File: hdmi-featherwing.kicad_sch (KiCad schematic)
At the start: 9 parts

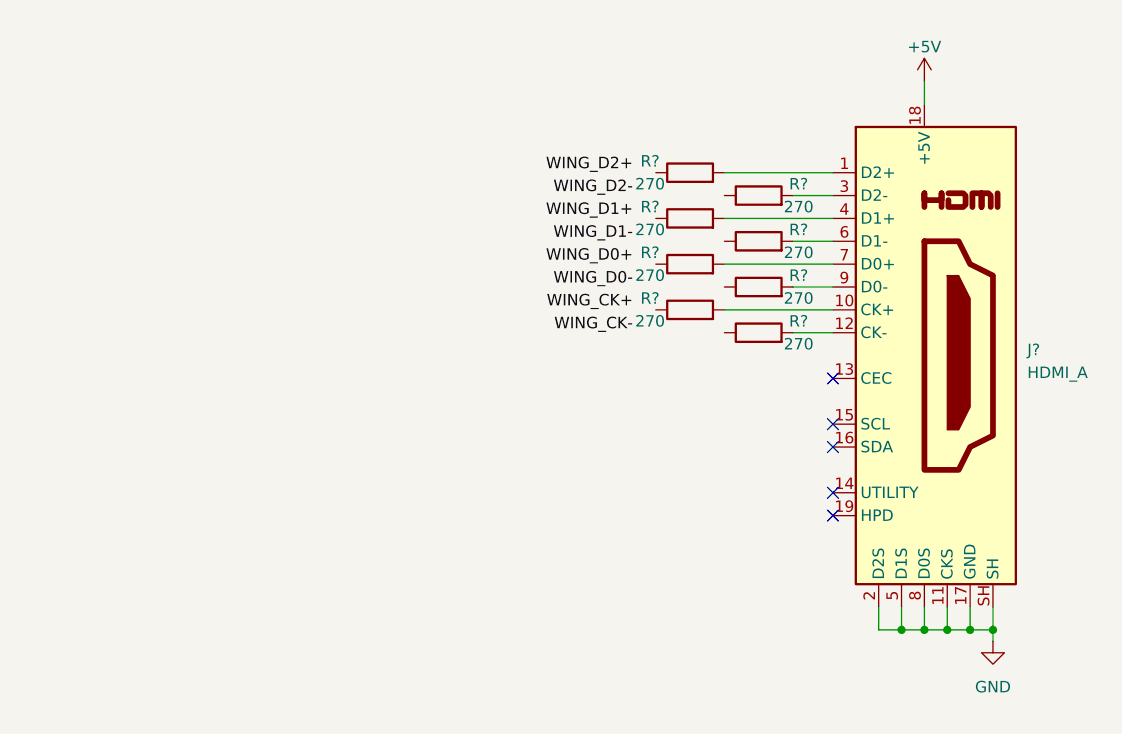
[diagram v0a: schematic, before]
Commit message: Add Feather to schematic
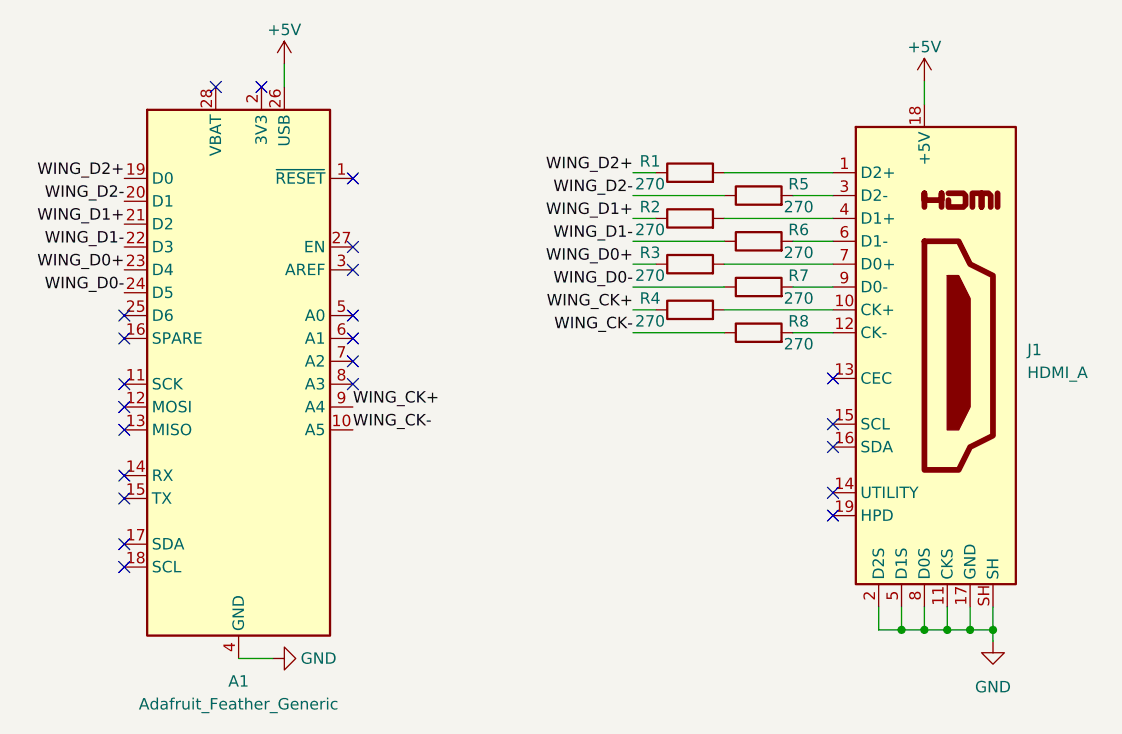
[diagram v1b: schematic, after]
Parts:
- added A1: Adafruit_Feather_Generic, Module:Adafruit_Feather, symbol MCU_Module:Adafruit_Feather_Generic
- gave numbers to parts that had none: 9
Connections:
- net +5V: now also A1.26 (USB)
- net GND: now also A1.4 (GND)
- net WING_CK+: now also R4.1, A1.9 (A4)
- net WING_CK-: now also R8.1, A1.10 (A5)
- net WING_D0+: now also R3.1, A1.23 (D4)
- net WING_D0-: now also R7.1, A1.24 (D5)
- net WING_D1+: now also R2.1, A1.21 (D2)
- net WING_D1-: now also R6.1, A1.22 (D3)
- net WING_D2+: now also R1.1, A1.19 (D0)
- net WING_D2-: now also R5.1, A1.20 (D1)
- no-connect marks 5 -> 23

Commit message: Assign footprints
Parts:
- A1: footprint Module:Adafruit_Feather -> Module:Adafruit_Feather_WithMountingHoles
- R1, R2, R3, R4, R5, R6, R7, R8: footprint (none) -> Resistor_SMD:R_0805_2012Metric
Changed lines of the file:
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@@
     (property "Reference" "R1" (id 0) (at 156.21 60.96 90))
     (property "Value" "270" (id 1) (at 156.21 63.5 90))
-    (property "Footprint" "" (id 2) (at 160.655 64.008 90)
+    (property "Footprint" "Resistor_SMD:R_0805_2012Metric" (id 2) (at 160.655 64.008 90)
       (effects (font (size 1.27 1.27)) hide)
     )
@@
     (property "Reference" "R2" (id 0) (at 156.21 66.04 90))
     (property "Value" "270" (id 1) (at 156.21 68.58 90))
-    (property "Footprint" "" (id 2) (at 160.655 69.088 90)
+    (property "Footprint" "Resistor_SMD:R_0805_2012Metric" (id 2) (at 160.655 69.088 90)
       (effects (font (size 1.27 1.27)) hide)
     )
@@
     (property "Reference" "R3" (id 0) (at 156.21 71.12 90))
     (property "Value" "270" (id 1) (at 156.21 73.66 90))
-    (property "Footprint" "" (id 2) (at 160.655 74.168 90)
+    (property "Footprint" "Resistor_SMD:R_0805_2012Metric" (id 2) (at 160.655 74.168 90)
       (effects (font (size 1.27 1.27)) hide)
     )
@@
     (property "Reference" "R4" (id 0) (at 156.21 76.2 90))
     (property "Value" "270" (id 1) (at 156.21 78.74 90))
-    (property "Footprint" "" (id 2) (at 160.655 79.248 90)
+    (property "Footprint" "Resistor_SMD:R_0805_2012Metric" (id 2) (at 160.655 79.248 90)
       (effects (font (size 1.27 1.27)) hide)
     )
@@
     (property "Reference" "R5" (id 0) (at 172.72 63.5 90))
     (property "Value" "270" (id 1) (at 172.72 66.04 90))
-    (property "Footprint" "" (id 2) (at 168.275 66.548 90)
+    (property "Footprint" "Resistor_SMD:R_0805_2012Metric" (id 2) (at 168.275 66.548 90)
       (effects (font (size 1.27 1.27)) hide)
     )
@@
     (property "Reference" "R6" (id 0) (at 172.72 68.58 90))
     (property "Value" "270" (id 1) (at 172.72 71.12 90))
-    (property "Footprint" "" (id 2) (at 168.275 71.628 90)
+    (property "Footprint" "Resistor_SMD:R_0805_2012Metric" (id 2) (at 168.275 71.628 90)
       (effects (font (size 1.27 1.27)) hide)
     )
@@
     (property "Reference" "R7" (id 0) (at 172.72 73.66 90))
     (property "Value" "270" (id 1) (at 172.72 76.2 90))
-    (property "Footprint" "" (id 2) (at 168.275 76.708 90)
+    (property "Footprint" "Resistor_SMD:R_0805_2012Metric" (id 2) (at 168.275 76.708 90)
       (effects (font (size 1.27 1.27)) hide)
     )
@@
     (property "Reference" "R8" (id 0) (at 172.72 78.74 90))
     (property "Value" "270" (id 1) (at 172.72 81.28 90))
-    (property "Footprint" "" (id 2) (at 168.275 81.788 90)
+    (property "Footprint" "Resistor_SMD:R_0805_2012Metric" (id 2) (at 168.275 81.788 90)
       (effects (font (size 1.27 1.27)) hide)
     )
@@
     (property "Reference" "A1" (id 0) (at 110.49 118.745 0))
     (property "Value" "Adafruit_Feather_Generic" (id 1) (at 110.49 121.285 0))
-    (property "Footprint" "Module:Adafruit_Feather" (id 2) (at 113.03 117.475 0)
+    (property "Footprint" "Module:Adafruit_Feather_WithMountingHoles" (id 2) (at 113.03 117.475 0)
       (effects (font (size 1.27 1.27)) (justify left) hide)
     )
@@
     )
     (path "/3e967f1b-54c7-4065-ae92-6c0121775b5f"
-      (reference "A1") (unit 1) (value "Adafruit_Feather_Generic") (footprint "Module:Adafruit_Feather")
+      (reference "A1") (unit 1) (value "Adafruit_Feather_Generic") (footprint "Module:Adafruit_Feather_WithMountingHoles")
     )
     (path "/fe48d55d-272e-4f11-a1c3-2a9246c6f613"
@@
     )
     (path "/12095942-e316-43e6-8e91-820591daa66e"
-      (reference "R1") (unit 1) (value "270") (footprint "")
+      (reference "R1") (unit 1) (value "270") (footprint "Resistor_SMD:R_0805_2012Metric")
     )
     (path "/eeb927ea-8397-4c7d-9a56-27649363bfbf"
-      (reference "R2") (unit 1) (value "270") (footprint "")
+      (reference "R2") (unit 1) (value "270") (footprint "Resistor_SMD:R_0805_2012Metric")
     )
     (path "/d3d37288-f0ba-4fe0-9fd0-56afc5bb6815"
-      (reference "R3") (unit 1) (value "270") (footprint "")
+      (reference "R3") (unit 1) (value "270") (footprint "Resistor_SMD:R_0805_2012Metric")
     )
     (path "/c8b38ce0-8172-4ca5-b311-7991ef2356c2"
-      (reference "R4") (unit 1) (value "270") (footprint "")
+      (reference "R4") (unit 1) (value "270") (footprint "Resistor_SMD:R_0805_2012Metric")
     )
     (path "/55298014-470c-4e6b-a6bd-6f35e8695295"
-      (reference "R5") (unit 1) (value "270") (footprint "")
+      (reference "R5") (unit 1) (value "270") (footprint "Resistor_SMD:R_0805_2012Metric")
     )
     (path "/692d872f-84be-419d-83c1-adc9ca84bc76"
-      (reference "R6") (unit 1) (value "270") (footprint "")
+      (reference "R6") (unit 1) (value "270") (footprint "Resistor_SMD:R_0805_2012Metric")
     )
     (path "/1725c309-b4c5-44b0-b5f8-36484d1f71d5"
-      (reference "R7") (unit 1) (value "270") (footprint "")
+      (reference "R7") (unit 1) (value "270") (footprint "Resistor_SMD:R_0805_2012Metric")
     )
     (path "/f3c2cf24-508f-45aa-96e8-0cfa5e7c4c3d"
-      (reference "R8") (unit 1) (value "270") (footprint "")
-    )
-  )
+      (reference "R8") (unit 1) (value "270") (footprint "Resistor_SMD:R_0805_2012Metric")
+    )
+  )

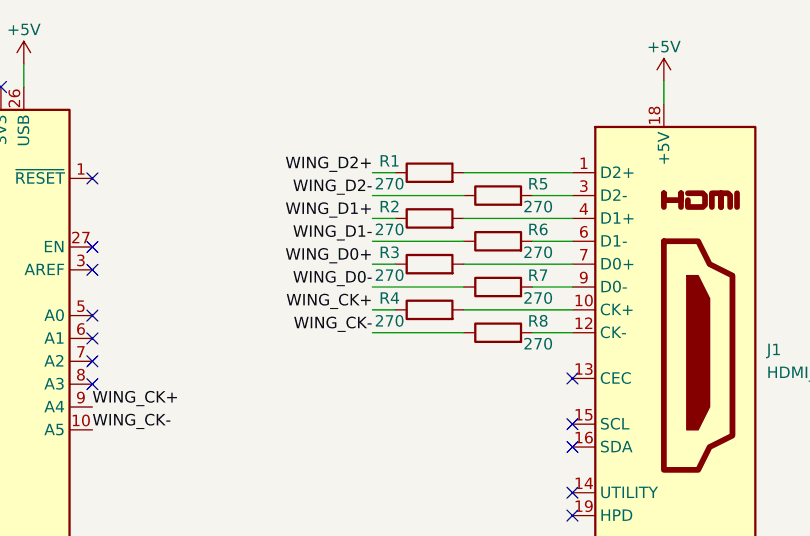
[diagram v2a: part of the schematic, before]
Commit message: Label differential pair nets
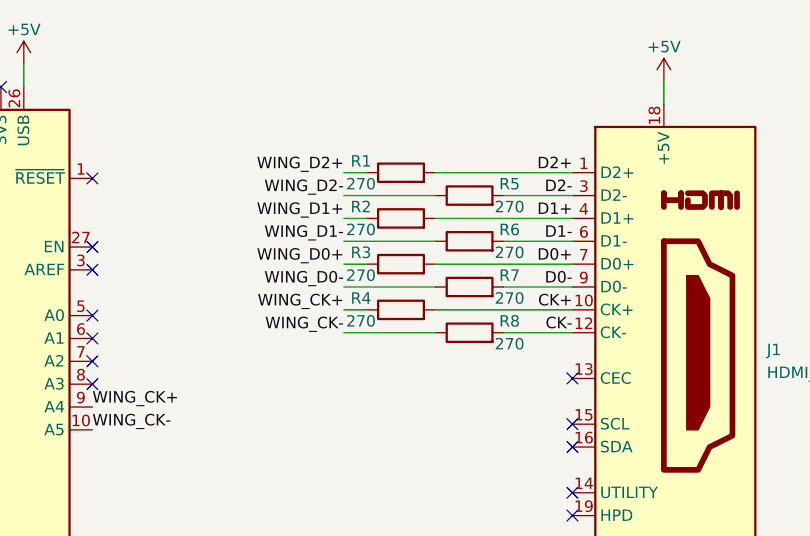
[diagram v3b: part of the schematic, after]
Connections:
- net D2+: now reaches J1.1 (D2+), R1.2
- net D0-: now reaches J1.9 (D0-), R7.2
- net D2-: now reaches J1.3 (D2-), R5.2
- net D1-: now reaches J1.6 (D1-), R6.2
- net CK+: now reaches J1.10 (CK+), R4.2
- net D0+: now reaches J1.7 (D0+), R3.2
- net D1+: now reaches J1.4 (D1+), R2.2
- net CK-: now reaches J1.12 (CK-), R8.2
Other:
- moved on the sheet: R1, R2, R3, R4, R5, R6, R7, R8

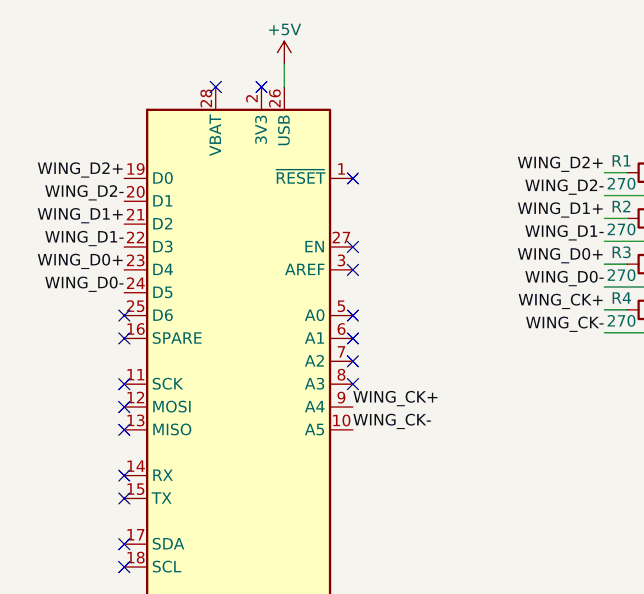
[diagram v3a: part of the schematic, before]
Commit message: Route resistors
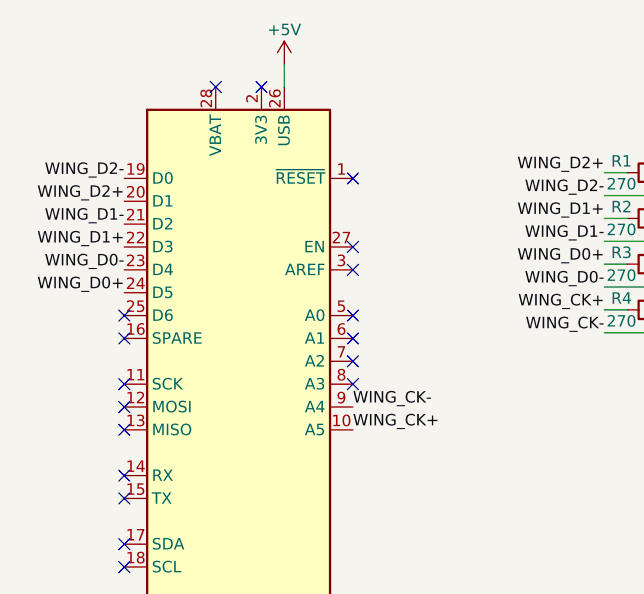
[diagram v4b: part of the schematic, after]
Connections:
- net WING_CK+: now also A1.10 (A5); no longer A1.9 (A4)
- net WING_CK-: now also A1.9 (A4); no longer A1.10 (A5)
- net WING_D0+: now also A1.24 (D5); no longer A1.23 (D4)
- net WING_D0-: now also A1.23 (D4); no longer A1.24 (D5)
- net WING_D1+: now also A1.22 (D3); no longer A1.21 (D2)
- net WING_D1-: now also A1.21 (D2); no longer A1.22 (D3)
- net WING_D2+: now also A1.20 (D1); no longer A1.19 (D0)
- net WING_D2-: now also A1.19 (D0); no longer A1.20 (D1)
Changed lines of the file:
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@@
     (stroke (width 0) (type solid) (color 0 0 0 0))
   )
-  (label "WING_D2+" (at 97.79 62.865 180)
+  (label "WING_D2-" (at 97.79 62.865 180)
     (effects (font (size 1.27 1.27)) (justify right bottom))
   )
-  (label "WING_D2-" (at 97.79 65.405 180)
+  (label "WING_D2+" (at 97.79 65.405 180)
     (effects (font (size 1.27 1.27)) (justify right bottom))
   )
-  (label "WING_D1+" (at 97.79 67.945 180)
+  (label "WING_D1-" (at 97.79 67.945 180)
     (effects (font (size 1.27 1.27)) (justify right bottom))
   )
-  (label "WING_D1-" (at 97.79 70.485 180)
+  (label "WING_D1+" (at 97.79 70.485 180)
     (effects (font (size 1.27 1.27)) (justify right bottom))
   )
-  (label "WING_D0+" (at 97.79 73.025 180)
+  (label "WING_D0-" (at 97.79 73.025 180)
     (effects (font (size 1.27 1.27)) (justify right bottom))
   )
-  (label "WING_D0-" (at 97.79 75.565 180)
+  (label "WING_D0+" (at 97.79 75.565 180)
     (effects (font (size 1.27 1.27)) (justify right bottom))
   )
-  (label "WING_CK+" (at 123.19 88.265 0)
+  (label "WING_CK-" (at 123.19 88.265 0)
     (effects (font (size 1.27 1.27)) (justify left bottom))
   )
-  (label "WING_CK-" (at 123.19 90.805 0)
+  (label "WING_CK+" (at 123.19 90.805 0)
     (effects (font (size 1.27 1.27)) (justify left bottom))
   )

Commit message: Add product codes for assembly
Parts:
- A1: now left out of the parts list
- J1: LCSC (none) -> C711354
- R1, R2, R3, R4, R5, R6, R7, R8: LCSC (none) -> C17590
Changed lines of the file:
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@@
+      (effects (font (size 1.27 1.27)) hide)
+    )
+    (property "LCSC" "C17590" (id 4) (at 157.48 62.23 90)
       (effects (font (size 1.27 1.27)) hide)
     )
@@
       (effects (font (size 1.27 1.27)) hide)
     )
+    (property "LCSC" "C17590" (id 4) (at 157.48 67.31 90)
+      (effects (font (size 1.27 1.27)) hide)
+    )
     (pin "1")
     (pin "2")
@@
     )
     (property "Datasheet" "~" (id 3) (at 157.48 72.39 0)
+      (effects (font (size 1.27 1.27)) hide)
+    )
+    (property "LCSC" "C17590" (id 4) (at 157.48 72.39 90)
       (effects (font (size 1.27 1.27)) hide)
     )
@@
       (effects (font (size 1.27 1.27)) hide)
     )
+    (property "LCSC" "C17590" (id 4) (at 157.48 77.47 90)
+      (effects (font (size 1.27 1.27)) hide)
+    )
     (pin "1")
     (pin "2")
@@
     )
     (property "Datasheet" "~" (id 3) (at 165.1 64.77 0)
+      (effects (font (size 1.27 1.27)) hide)
+    )
+    (property "LCSC" "C17590" (id 4) (at 165.1 64.77 90)
       (effects (font (size 1.27 1.27)) hide)
     )
@@
       (effects (font (size 1.27 1.27)) hide)
     )
+    (property "LCSC" "C17590" (id 4) (at 165.1 69.85 90)
+      (effects (font (size 1.27 1.27)) hide)
+    )
     (pin "1")
     (pin "2")
@@
       (effects (font (size 1.27 1.27)) hide)
     )
+    (property "LCSC" "C17590" (id 4) (at 165.1 74.93 90)
+      (effects (font (size 1.27 1.27)) hide)
+    )
     (pin "1")
     (pin "2")
@@
     )
     (property "Datasheet" "~" (id 3) (at 165.1 80.01 0)
+      (effects (font (size 1.27 1.27)) hide)
+    )
+    (property "LCSC" "C17590" (id 4) (at 165.1 80.01 90)
       (effects (font (size 1.27 1.27)) hide)
     )
@@
     )
     (property "Datasheet" "https://en.wikipedia.org/wiki/HDMI" (id 3) (at 187.325 82.55 0)
+      (effects (font (size 1.27 1.27)) hide)
+    )
+    (property "LCSC" "C711354" (id 4) (at 186.69 82.55 0)
       (effects (font (size 1.27 1.27)) hide)
     )
@@
   )
   (symbol (lib_id "MCU_Module:Adafruit_Feather_Generic") (at 110.49 83.185 0) (unit 1)
-    (in_bom yes) (on_board yes)
+    (in_bom no) (on_board yes)
     (property "Reference" "A1" (id 0) (at 110.49 118.745 0))
     (property "Value" "Adafruit_Feather_Generic" (id 1) (at 110.49 121.285 0))
